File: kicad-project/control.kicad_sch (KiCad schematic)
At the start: 34 parts, among them J1 Conn_02x04_Counter_Clockwise, J2 Conn_02x08_Counter_Clockwise, SW1 PRG_SW, SW2 RST_SW, SW3 HOME_SW, SW4 EN_SW, U1 W25Q16JVSS, U2 RP2040, Y1 12MHz

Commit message: hw: add fiducial to eeschema and change sw footprints
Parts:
- SW1, SW2, SW3, SW4: footprint Button_Switch_SMD:SW_SPST_PTS645 -> (none)
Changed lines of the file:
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@@
       (effects (font (size 1.27 1.27)) (justify left))
     )
-    (property "Footprint" "Button_Switch_SMD:SW_SPST_PTS645" (id 2) (at 34.29 90.17 0)
+    (property "Footprint" "" (id 2) (at 34.29 90.17 0)
       (effects (font (size 1.27 1.27)) hide)
     )
@@
       (effects (font (size 1.27 1.27)) (justify left))
     )
-    (property "Footprint" "Button_Switch_SMD:SW_SPST_PTS645" (id 2) (at 97.79 130.81 0)
+    (property "Footprint" "" (id 2) (at 97.79 130.81 0)
       (effects (font (size 1.27 1.27)) hide)
     )
@@
       (effects (font (size 1.27 1.27)) (justify left))
     )
-    (property "Footprint" "Button_Switch_SMD:SW_SPST_PTS645" (id 2) (at 19.05 182.88 0)
+    (property "Footprint" "" (id 2) (at 19.05 182.88 0)
       (effects (font (size 1.27 1.27)) hide)
     )
@@
       (effects (font (size 1.27 1.27)) (justify left))
     )
-    (property "Footprint" "Button_Switch_SMD:SW_SPST_PTS645" (id 2) (at 78.74 90.17 0)
-      (effects (font (size 1.27 1.27)) hide)
-    )
+    (property "Footprint" "" (id 2) (at 78.74 90.17 0)
+      (effects (font (size 1.27 1.27)) hide)
+    )

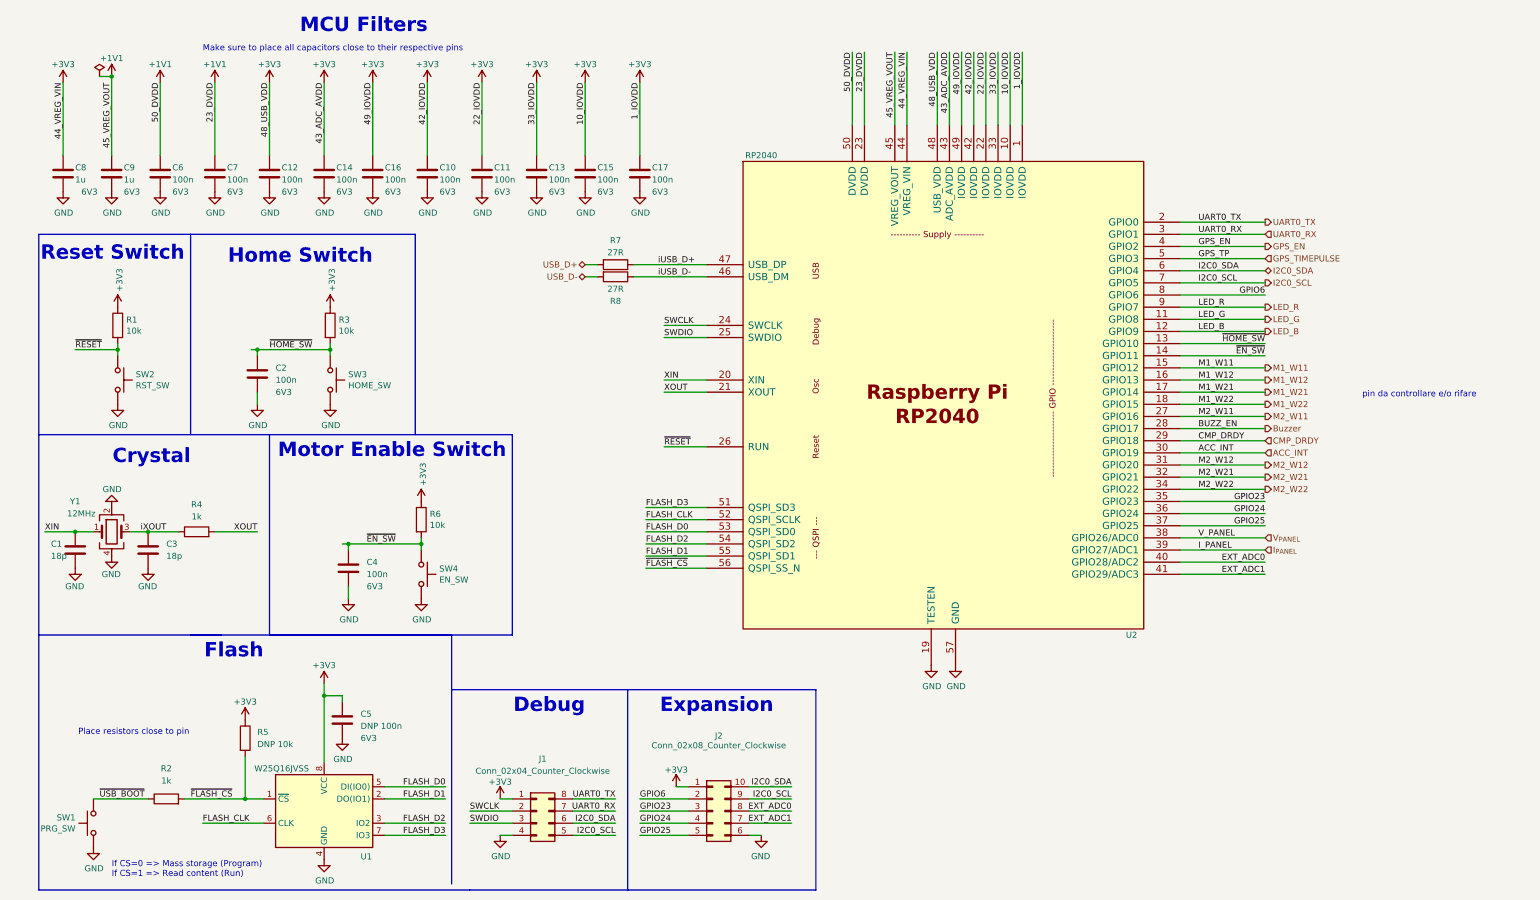
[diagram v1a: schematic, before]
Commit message: change mcu pins and optimize layout
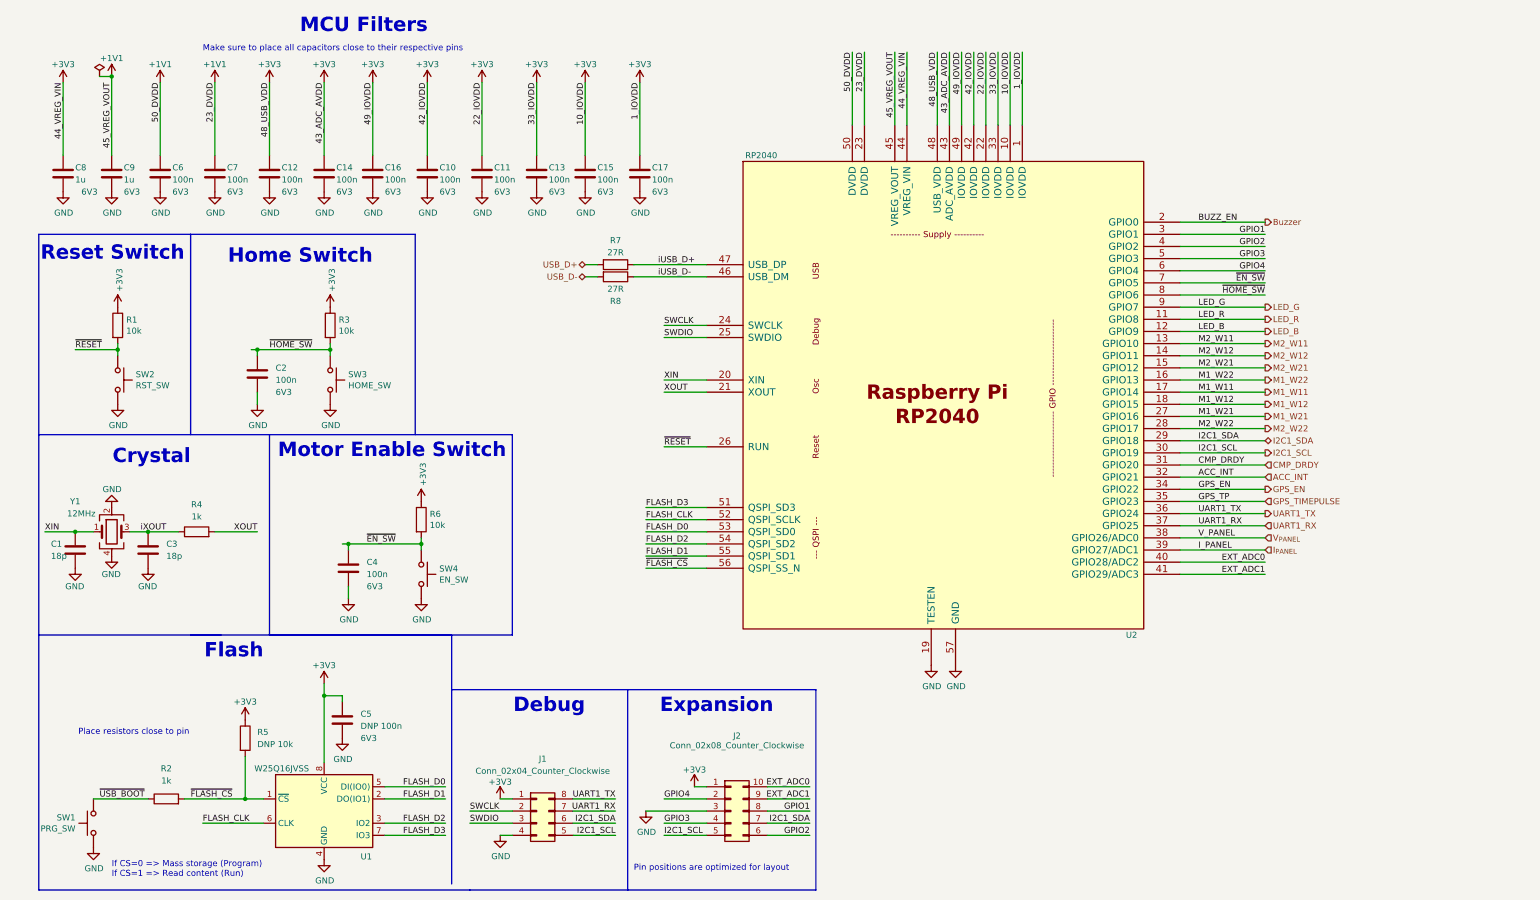
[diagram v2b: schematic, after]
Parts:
- SW1, SW2, SW3, SW4: footprint (none) -> Button_Switch_THT:SW_PUSH_6mm
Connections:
- net ACC_INT: now also U2.32 (GPIO21); no longer U2.30 (GPIO19)
- net Buzzer: now also U2.2 (GPIO0); no longer U2.28 (GPIO17)
- net CMP_DRDY: now also U2.31 (GPIO20); no longer U2.29 (GPIO18)
- net EXT_ADC0: now also J2.10 (Pin_10); no longer J2.8 (Pin_8)
- net EXT_ADC1: now also J2.9 (Pin_9); no longer J2.7 (Pin_7)
- net GND: now also J2.3 (Pin_3); no longer J2.6 (Pin_6)
- net GPS_EN: now also U2.34 (GPIO22); no longer U2.4 (GPIO2)
- net GPS_TIMEPULSE: now also U2.35 (GPIO23); no longer U2.5 (GPIO3)
- net LED_G: now also U2.9 (GPIO7); no longer U2.11 (GPIO8)
- net LED_R: now also U2.11 (GPIO8); no longer U2.9 (GPIO7)
- net M1_W11: now also U2.17 (GPIO14); no longer U2.15 (GPIO12)
- net M1_W12: now also U2.18 (GPIO15); no longer U2.16 (GPIO13)
- net M1_W21: now also U2.27 (GPIO16); no longer U2.17 (GPIO14)
- net M1_W22: now also U2.16 (GPIO13); no longer U2.18 (GPIO15)
- net M2_W11: now also U2.13 (GPIO10); no longer U2.27 (GPIO16)
- net M2_W12: now also U2.14 (GPIO11); no longer U2.31 (GPIO20)
- net M2_W21: now also U2.15 (GPIO12); no longer U2.32 (GPIO21)
- net M2_W22: now also U2.28 (GPIO17); no longer U2.34 (GPIO22)
- net ~{EN_SW}: now also U2.7 (GPIO5); no longer U2.14 (GPIO11)
- net ~{HOME_SW}: now also U2.8 (GPIO6); no longer U2.13 (GPIO10)
- removed net GPIO23: J2.3 (Pin_3), U2.35 (GPIO23)
- net GPIO24 renamed GPIO3
- net GPIO3: now also U2.5 (GPIO3); no longer U2.36 (GPIO24)
- net GPIO25 renamed I2C1_SCL
- net I2C1_SCL: now also J1.5 (Pin_5), U2.30 (GPIO19); no longer U2.37 (GPIO25)
- net GPIO6 renamed GPIO4
- net GPIO4: now also U2.6 (GPIO4); no longer U2.8 (GPIO6)
- removed net I2C0_SCL: J1.5 (Pin_5), J2.9 (Pin_9), U2.7 (GPIO5)
- removed net I2C0_SDA: J1.6 (Pin_6), J2.10 (Pin_10), U2.6 (GPIO4)
- net UART0_RX renamed GPIO1
- net GPIO1: now also J2.8 (Pin_8); no longer J1.7 (Pin_7)
- net UART0_TX renamed UART1_TX
- net UART1_TX: now also U2.36 (GPIO24); no longer U2.2 (GPIO0)
- new net GPIO2: J2.6 (Pin_6), U2.4 (GPIO2)
- new net I2C1_SDA: J1.6 (Pin_6), J2.7 (Pin_7), U2.29 (GPIO18)
- new net UART1_RX: J1.7 (Pin_7), U2.37 (GPIO25)
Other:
- note added: "Pin positions are optimized for layout"
- note removed: "pin da controllare e/o rifare"
- moved on the sheet: J2

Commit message: hw: first round of routing
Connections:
- net M1_W22: now also U2.28 (GPIO17); no longer U2.16 (GPIO13)
- net M2_W22: now also U2.16 (GPIO13); no longer U2.28 (GPIO17)
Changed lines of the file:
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@@
     (effects (font (size 1.27 1.27)) (justify left bottom))
   )
-  (label "M1_W22" (at 255.27 90.17 0)
+  (label "M1_W22" (at 255.27 100.33 0)
     (effects (font (size 1.27 1.27)) (justify left bottom))
   )
@@
     (effects (font (size 1.27 1.27)) (justify right bottom))
   )
-  (label "M2_W22" (at 255.27 100.33 0)
+  (label "M2_W22" (at 255.27 90.17 0)
     (effects (font (size 1.27 1.27)) (justify left bottom))
   )
@@
     (effects (font (size 1.27 1.27)) (justify left))
   )
-  (hierarchical_label "M1_W22" (shape output) (at 269.24 90.17 0)
+  (hierarchical_label "M1_W22" (shape output) (at 269.24 100.33 0)
     (effects (font (size 1.27 1.27)) (justify left))
   )
@@
     (effects (font (size 1.27 1.27)) (justify left))
   )
-  (hierarchical_label "M2_W22" (shape output) (at 269.24 100.33 0)
-    (effects (font (size 1.27 1.27)) (justify left))
-  )
+  (hierarchical_label "M2_W22" (shape output) (at 269.24 90.17 0)
+    (effects (font (size 1.27 1.27)) (justify left))
+  )

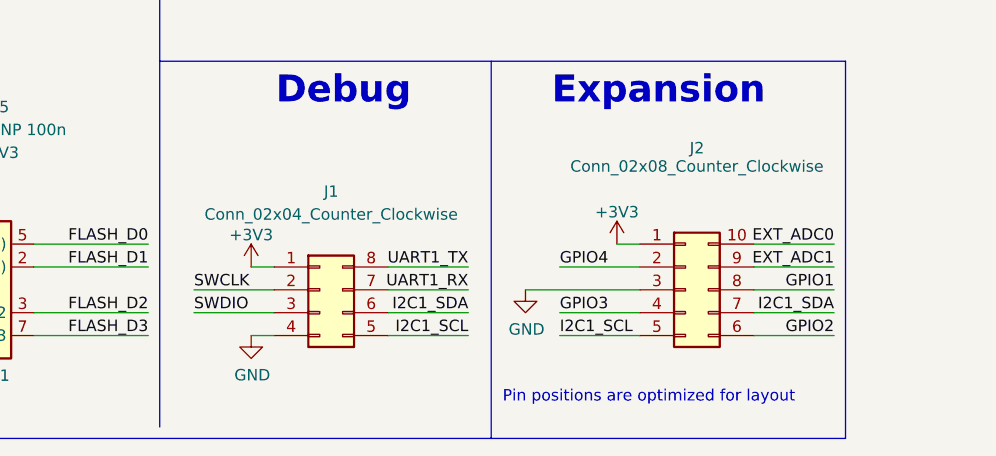
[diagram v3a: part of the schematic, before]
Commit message: hw: finalize routing (dbg uart missing)
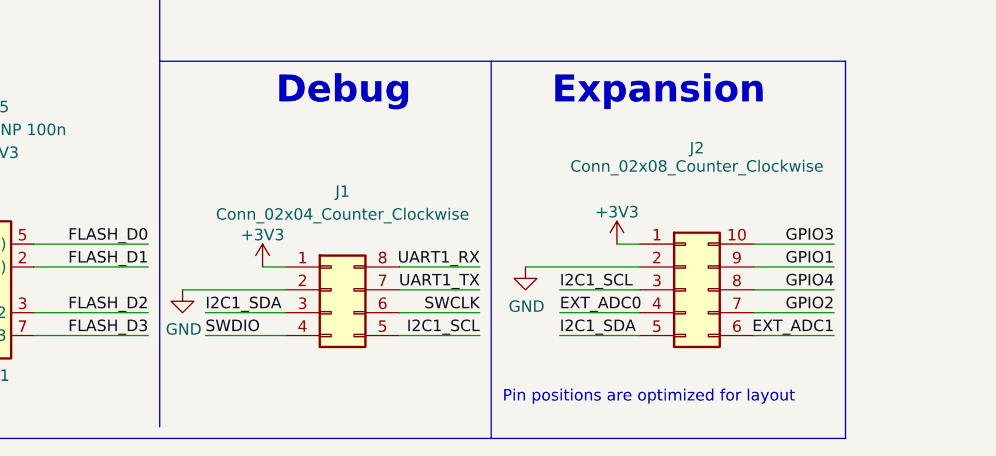
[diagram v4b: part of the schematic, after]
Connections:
- net EXT_ADC0: now also J2.4 (Pin_4); no longer J2.10 (Pin_10)
- net EXT_ADC1: now also J2.6 (Pin_6); no longer J2.9 (Pin_9)
- net GND: now also J1.2 (Pin_2), J2.2 (Pin_2); no longer J1.4 (Pin_4), J2.3 (Pin_3)
- net GPIO1: now also J2.9 (Pin_9); no longer J2.8 (Pin_8)
- net GPIO2: now also J2.7 (Pin_7); no longer J2.6 (Pin_6)
- net GPIO3: now also J2.10 (Pin_10); no longer J2.4 (Pin_4)
- net GPIO4: now also J2.8 (Pin_8); no longer J2.2 (Pin_2)
- net I2C1_SCL: now also J2.3 (Pin_3); no longer J2.5 (Pin_5)
- net I2C1_SDA: now also J1.3 (Pin_3), J2.5 (Pin_5); no longer J1.6 (Pin_6), J2.7 (Pin_7)
- net SWCLK: now also J1.6 (Pin_6); no longer J1.2 (Pin_2)
- net SWDIO: now also J1.4 (Pin_4); no longer J1.3 (Pin_3)
- net UART1_RX: now also J1.8 (Pin_8); no longer J1.7 (Pin_7)
- net UART1_TX: now also J1.7 (Pin_7); no longer J1.8 (Pin_8)
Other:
- moved on the sheet: J1

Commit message: hw: final changes
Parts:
- removed J1: Conn_02x04_Counter_Clockwise, Connector_PinHeader_2.54mm:PinHeader_2x04_P2.54mm_Vertical, symbol Connector_Generic:Conn_02x04_Counter_Clockwise
- added J1: (no value), symbol Connector_Generic:Conn_02x03_Counter_Clockwise
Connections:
- net +3V3: now also J1.1 (Pin_1)
- net GND: now also J1.2 (Pin_2)
- net I2C1_SCL: now also J1.5 (Pin_5)
- net I2C1_SDA: now also J1.3 (Pin_3)
- net SWCLK: now also J1.6 (Pin_6)
- net SWDIO: now also J1.4 (Pin_4)

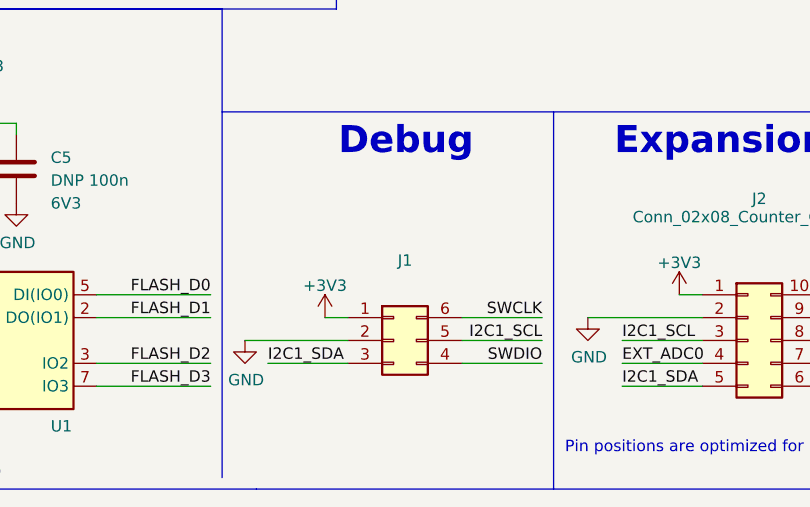
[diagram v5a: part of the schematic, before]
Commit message: hw: add sensing resistance values
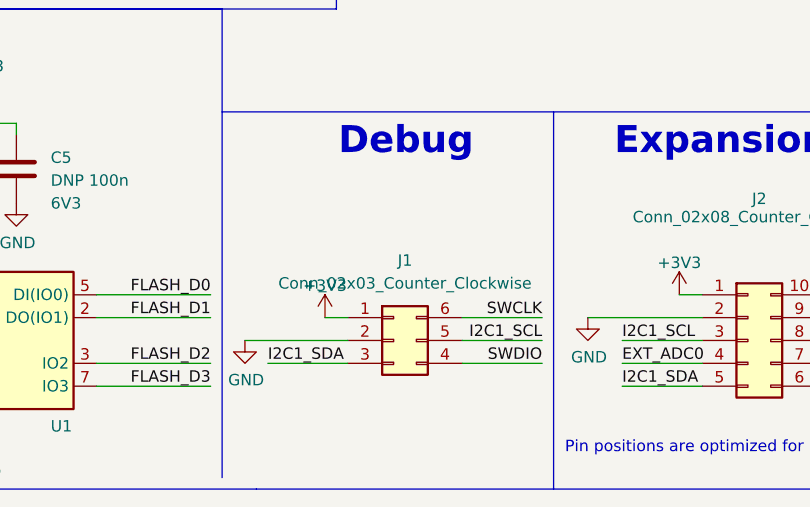
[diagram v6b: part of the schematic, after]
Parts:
- J1: value (none) -> Conn_02x03_Counter_Clockwise; footprint (none) -> Connector_PinHeader_2.54mm:PinHeader_2x03_P2.54mm_Vertical
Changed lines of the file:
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@@
     (in_bom yes) (on_board yes) (fields_autoplaced)
     (property "Reference" "J1" (id 0) (at 119.38 171.45 0))
-    (property "Value" "" (id 1) (at 119.38 173.99 0))
-    (property "Footprint" "" (id 2) (at 118.11 180.34 0)
+    (property "Value" "Conn_02x03_Counter_Clockwise" (id 1) (at 119.38 173.99 0))
+    (property "Footprint" "Connector_PinHeader_2.54mm:PinHeader_2x03_P2.54mm_Vertical" (id 2) (at 118.11 180.34 0)
       (effects (font (size 1.27 1.27)) hide)
     )

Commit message: hw: schematic updates
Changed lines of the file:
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@@
   (junction (at 73.66 83.82) (diameter 0) (color 0 0 0 0)
   )
-  (junction (at 27.94 26.67) (diameter 0) (color 0 0 0 0)
-  )
   (junction (at 72.39 156.21) (diameter 0) (color 0 0 0 0)
   )
@@
   )
   (wire (pts (xy 251.46 130.81) (xy 269.24 130.81))
-    (stroke (width 0) (type default) (color 0 0 0 0))
-  )
-  (wire (pts (xy 25.4 26.67) (xy 27.94 26.67))
     (stroke (width 0) (type default) (color 0 0 0 0))
   )
@@
     (pin "2")
   )
-  (symbol (lib_id "power:PWR_FLAG") (at 25.4 26.67 0) (unit 1)
-    (in_bom yes) (on_board yes)
-    (property "Reference" "#FLG0101" (id 0) (at 25.4 24.765 0)
-      (effects (font (size 1.27 1.27)) hide)
-    )
-    (property "Value" "PWR_FLAG" (id 1) (at 25.4 24.13 90)
+  (symbol (lib_id "power:PWR_FLAG") (at 191.77 21.59 0) (unit 1)
+    (in_bom yes) (on_board yes)
+    (property "Reference" "#FLG0101" (id 0) (at 191.77 19.685 0)
+      (effects (font (size 1.27 1.27)) hide)
+    )
+    (property "Value" "PWR_FLAG" (id 1) (at 191.77 19.05 90)
       (effects (font (size 1.27 1.27)) (justify left) hide)
     )
-    (property "Footprint" "" (id 2) (at 25.4 26.67 0)
-      (effects (font (size 1.27 1.27)) hide)
-    )
-    (property "Datasheet" "~" (id 3) (at 25.4 26.67 0)
-      (effects (font (size 1.27 1.27)) hide)
-    )
+    (property "Footprint" "" (id 2) (at 191.77 21.59 0)
+      (effects (font (size 1.27 1.27)) hide)
+    )
+    (property "Datasheet" "~" (id 3) (at 191.77 21.59 0)
+      (effects (font (size 1.27 1.27)) hide)
+    )
